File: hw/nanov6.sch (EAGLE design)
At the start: 28 parts, among them CON1 503548-1220, J1 M08X2, Q4 BSS138, U1 TPS622XX

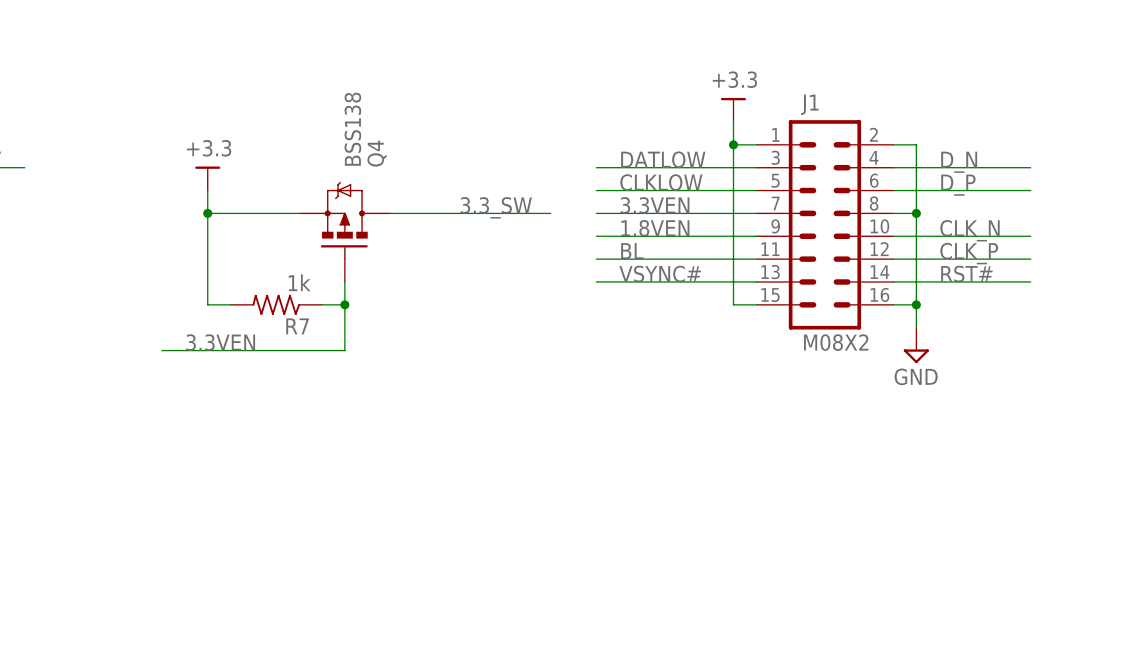
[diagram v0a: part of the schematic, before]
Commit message: add pulldown to RST#, make 3.3VEN active-high. Resolves #471, refs #469.
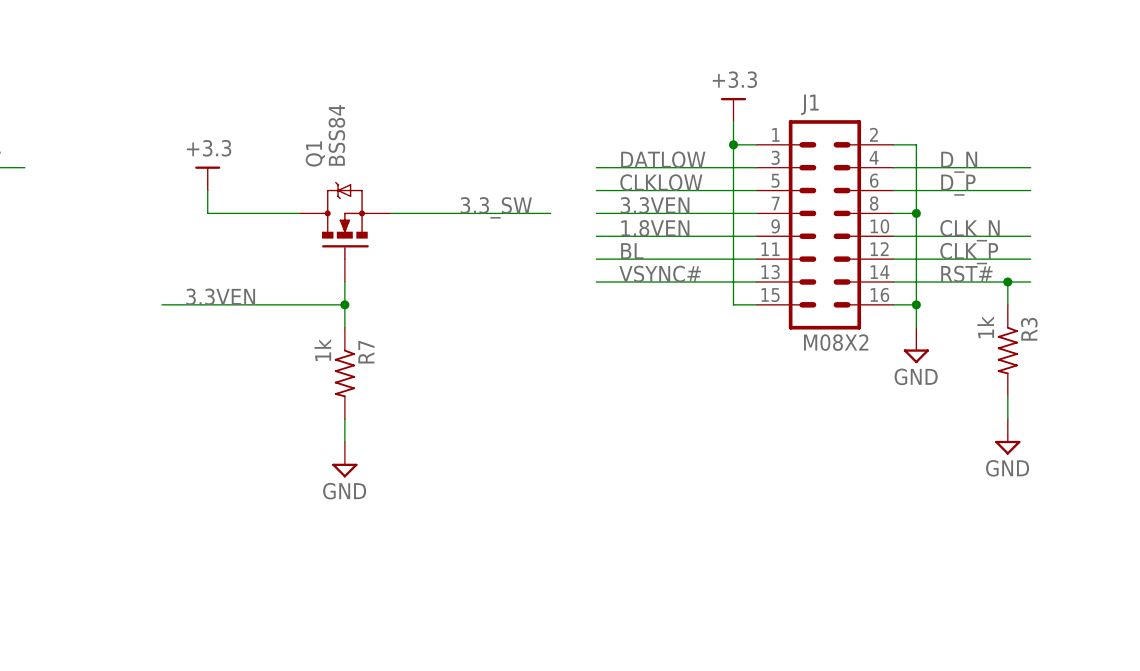
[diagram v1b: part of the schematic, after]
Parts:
- removed Q4: BSS138, SparkFun:MOSFET-PCHANNELSOT23
- added Q1: BSS84, SparkFun:MOSFET-NCHANNELSMD
- added R3: 1k, rcl:R-US_R0805
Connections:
- net +3.3: now also Q1.D; no longer Q4.S, R7.2
- net 3.3VEN: now also Q1.G; no longer Q4.G
- net 3.3_SW: now also Q1.S; no longer Q4.D
- net GND: now also R3.2, R7.2
- net RST#: now also R3.1
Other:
- moved on the sheet: R7
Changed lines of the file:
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@@
 <part name="R13" library="rcl" deviceset="R-US_" device="R0805" value="0"/>
 <part name="U$4" library="ak-supply" deviceset="+3.3" device=""/>
-<part name="Q4" library="SparkFun" deviceset="MOSFET-PCHANNEL" device="SOT23" value="BSS138"/>
 <part name="R7" library="rcl" deviceset="R-US_" device="R0805" value="1k"/>
 <part name="U2" library="ak-misc" deviceset="TLV61220" device=""/>
@@
 <part name="U$11" library="ak-misc" deviceset="MOUNTING_HOLE" device="125"/>
 <part name="U$15" library="ak-misc" deviceset="MOUNTING_HOLE" device="125"/>
+<part name="Q1" library="SparkFun" deviceset="MOSFET-NCHANNEL" device="SMD" value="BSS84"/>
+<part name="U$16" library="ak-supply" deviceset="GND" device=""/>
+<part name="R3" library="rcl" deviceset="R-US_" device="R0805" value="1k"/>
+<part name="U$17" library="ak-supply" deviceset="GND" device=""/>
 </parts>
 <sheets>
@@
 <instance part="R13" gate="G$1" x="101.6" y="147.32" rot="R180"/>
 <instance part="U$4" gate="G$1" x="208.28" y="152.4"/>
-<instance part="Q4" gate="G$1" x="223.52" y="147.32" rot="MR90"/>
-<instance part="R7" gate="G$1" x="215.9" y="137.16" rot="R180"/>
+<instance part="R7" gate="G$1" x="223.52" y="129.54" rot="R270"/>
 <instance part="U2" gate="G$1" x="137.16" y="106.68"/>
 <instance part="R8" gate="G$1" x="154.94" y="93.98" rot="R270"/>
@@
 <instance part="U$11" gate="G$1" x="134.62" y="30.48"/>
 <instance part="U$15" gate="G$1" x="139.7" y="30.48"/>
+<instance part="Q1" gate="G$1" x="223.52" y="147.32" rot="R90"/>
+<instance part="U$16" gate="G$1" x="223.52" y="119.38"/>
+<instance part="R3" gate="G$1" x="297.18" y="132.08" rot="R270"/>
+<instance part="U$17" gate="G$1" x="297.18" y="121.92"/>
 </instances>
 <busses>
@@
 <junction x="266.7" y="25.4"/>
 </segment>
+<segment>
+<pinref part="U$16" gate="G$1" pin="GND"/>
+<pinref part="R7" gate="G$1" pin="2"/>
+<wire x1="223.52" y1="121.92" x2="223.52" y2="124.46" width="0.1524" layer="91"/>
+</segment>
+<segment>
+<pinref part="U$17" gate="G$1" pin="GND"/>
+<pinref part="R3" gate="G$1" pin="2"/>
+<wire x1="297.18" y1="124.46" x2="297.18" y2="127" width="0.1524" layer="91"/>
+</segment>
 </net>
 <net name="CLKLOW" class="0">
@@
 </segment>
 <segment>
-<pinref part="Q4" gate="G$1" pin="D"/>
 <label x="236.22" y="147.32" size="1.778" layer="95"/>
 <wire x1="228.6" y1="147.32" x2="246.38" y2="147.32" width="0.1524" layer="91"/>
+<pinref part="Q1" gate="G$1" pin="S"/>
 </segment>
 </net>
@@
 <segment>
 <pinref part="J1" gate="G$1" pin="14"/>
-<wire x1="284.48" y1="139.7" x2="299.72" y2="139.7" width="0.1524" layer="91"/>
+<wire x1="284.48" y1="139.7" x2="297.18" y2="139.7" width="0.1524" layer="91"/>
 <label x="289.56" y="139.7" size="1.778" layer="95"/>
+<pinref part="R3" gate="G$1" pin="1"/>
+<wire x1="297.18" y1="139.7" x2="299.72" y2="139.7" width="0.1524" layer="91"/>
+<wire x1="297.18" y1="137.16" x2="297.18" y2="139.7" width="0.1524" layer="91"/>
+<junction x="297.18" y="139.7"/>
 </segment>
 </net>
@@
 </segment>
 <segment>
-<pinref part="Q4" gate="G$1" pin="S"/>
-<pinref part="R7" gate="G$1" pin="2"/>
-<wire x1="210.82" y1="137.16" x2="208.28" y2="137.16" width="0.1524" layer="91"/>
-<wire x1="208.28" y1="137.16" x2="208.28" y2="147.32" width="0.1524" layer="91"/>
 <pinref part="U$4" gate="G$1" pin="+3.3"/>
 <wire x1="208.28" y1="147.32" x2="218.44" y2="147.32" width="0.1524" layer="91"/>
 <wire x1="208.28" y1="149.86" x2="208.28" y2="147.32" width="0.1524" layer="91"/>
-<junction x="208.28" y="147.32"/>
+<pinref part="Q1" gate="G$1" pin="D"/>
 </segment>
 <segment>
@@
 <segment>
 <pinref part="R7" gate="G$1" pin="1"/>
-<wire x1="220.98" y1="137.16" x2="223.52" y2="137.16" width="0.1524" layer="91"/>
-<pinref part="Q4" gate="G$1" pin="G"/>
+<wire x1="223.52" y1="134.62" x2="223.52" y2="137.16" width="0.1524" layer="91"/>
 <wire x1="223.52" y1="139.7" x2="223.52" y2="137.16" width="0.1524" layer="91"/>
-<wire x1="223.52" y1="137.16" x2="223.52" y2="132.08" width="0.1524" layer="91"/>
 <junction x="223.52" y="137.16"/>
-<wire x1="223.52" y1="132.08" x2="203.2" y2="132.08" width="0.1524" layer="91"/>
-<label x="205.74" y="132.08" size="1.778" layer="95"/>
-</segment>
-<segment>
+<wire x1="223.52" y1="137.16" x2="203.2" y2="137.16" width="0.1524" layer="91"/>
+<label x="205.74" y="137.16" size="1.778" layer="95"/>
+<pinref part="Q1" gate="G$1" pin="G"/>
+</segment>
+<segment>

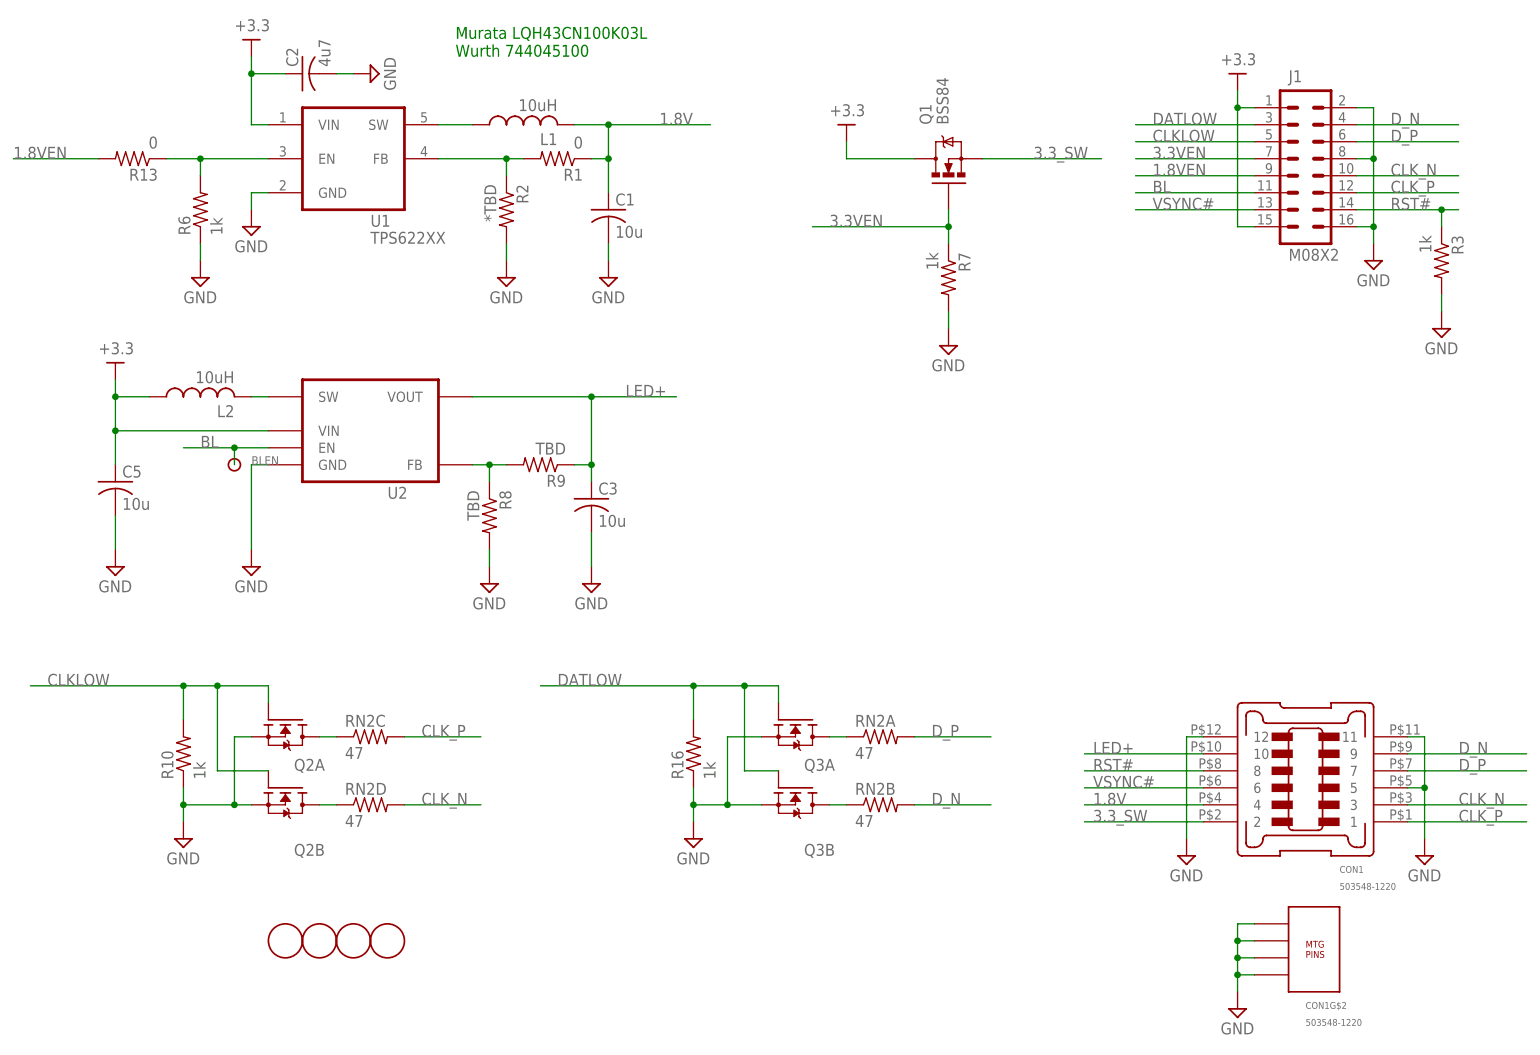
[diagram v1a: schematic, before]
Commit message: add pulldown to BLEN. Resolves #469.
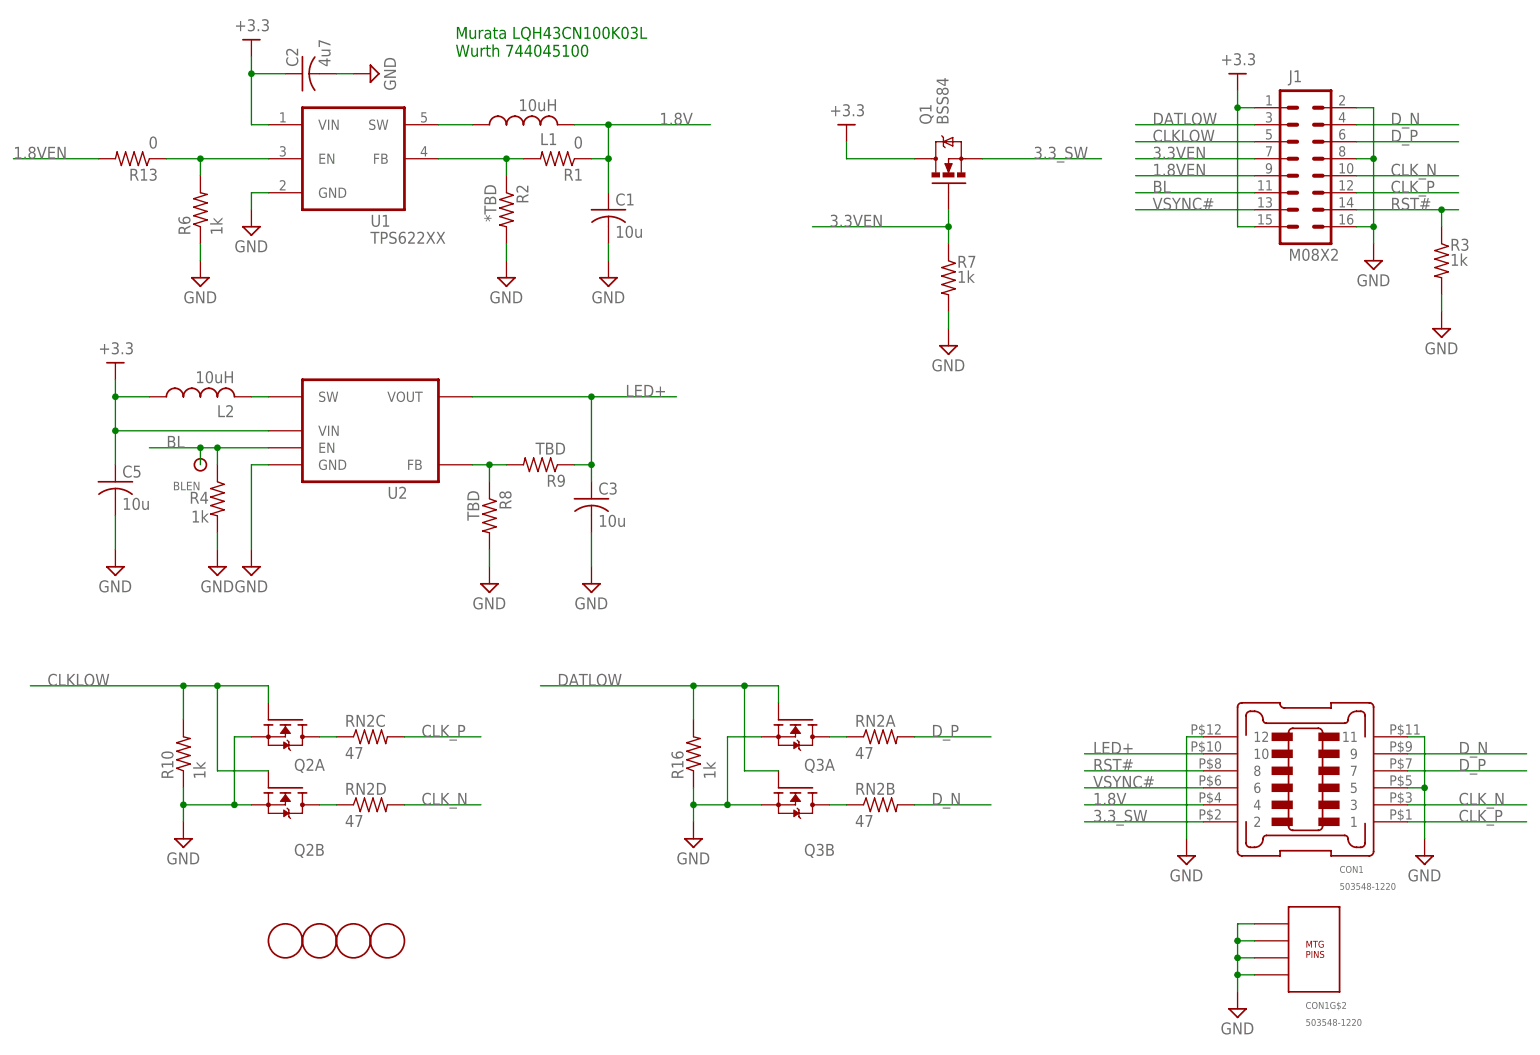
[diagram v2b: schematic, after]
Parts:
- added R4: 1k, rcl:R-US_R0805
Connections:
- net BL: now also R4.1
- net GND: now also R4.2
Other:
- moved on the sheet: BLEN
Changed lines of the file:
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@@
 <part name="R3" library="rcl" deviceset="R-US_" device="R0805" value="1k"/>
 <part name="U$17" library="ak-supply" deviceset="GND" device=""/>
+<part name="R4" library="rcl" deviceset="R-US_" device="R0805" value="1k"/>
+<part name="U$18" library="ak-supply" deviceset="GND" device=""/>
 </parts>
 <sheets>
@@
 <instance part="R13" gate="G$1" x="101.6" y="147.32" rot="R180"/>
 <instance part="U$4" gate="G$1" x="208.28" y="152.4"/>
-<instance part="R7" gate="G$1" x="223.52" y="129.54" rot="R270"/>
+<instance part="R7" gate="G$1" x="223.52" y="129.54" smashed="yes" rot="R270">
+<attribute name="NAME" x="224.79" y="131.0386" size="1.778" layer="95"/>
+<attribute name="VALUE" x="224.79" y="128.778" size="1.778" layer="96"/>
+</instance>
 <instance part="U2" gate="G$1" x="137.16" y="106.68"/>
 <instance part="R8" gate="G$1" x="154.94" y="93.98" rot="R270"/>
@@
 <instance part="U$13" gate="G$1" x="99.06" y="116.84"/>
 <instance part="U$14" gate="G$1" x="266.7" y="160.02"/>
-<instance part="BLEN" gate="1" x="116.84" y="101.6"/>
+<instance part="BLEN" gate="1" x="111.76" y="101.6" smashed="yes">
+<attribute name="NAME" x="111.76" y="99.06" size="1.27" layer="96" rot="R180"/>
+</instance>
 <instance part="CON1" gate="G$2" x="276.86" y="27.94"/>
 <instance part="U$5" gate="G$1" x="266.7" y="20.32"/>
@@
 <instance part="Q1" gate="G$1" x="223.52" y="147.32" rot="R90"/>
 <instance part="U$16" gate="G$1" x="223.52" y="119.38"/>
-<instance part="R3" gate="G$1" x="297.18" y="132.08" rot="R270"/>
+<instance part="R3" gate="G$1" x="297.18" y="132.08" smashed="yes" rot="R270">
+<attribute name="NAME" x="298.45" y="133.5786" size="1.778" layer="95"/>
+<attribute name="VALUE" x="298.45" y="131.318" size="1.778" layer="96"/>
+</instance>
 <instance part="U$17" gate="G$1" x="297.18" y="121.92"/>
+<instance part="R4" gate="G$1" x="114.3" y="96.52" smashed="yes" rot="R270">
+<attribute name="NAME" x="113.03" y="97.5614" size="1.778" layer="95" rot="R180"/>
+<attribute name="VALUE" x="113.03" y="94.742" size="1.778" layer="96" rot="R180"/>
+</instance>
+<instance part="U$18" gate="G$1" x="114.3" y="86.36"/>
 </instances>
 <busses>
@@
 <wire x1="297.18" y1="124.46" x2="297.18" y2="127" width="0.1524" layer="91"/>
 </segment>
+<segment>
+<pinref part="R4" gate="G$1" pin="2"/>
+<pinref part="U$18" gate="G$1" pin="GND"/>
+<wire x1="114.3" y1="91.44" x2="114.3" y2="88.9" width="0.1524" layer="91"/>
+</segment>
 </net>
 <net name="CLKLOW" class="0">
@@
 <segment>
 <pinref part="U2" gate="G$1" pin="EN"/>
-<wire x1="121.92" y1="104.14" x2="116.84" y2="104.14" width="0.1524" layer="91"/>
-<label x="111.76" y="104.14" size="1.778" layer="95"/>
+<wire x1="121.92" y1="104.14" x2="114.3" y2="104.14" width="0.1524" layer="91"/>
+<label x="106.68" y="104.14" size="1.778" layer="95"/>
 <pinref part="BLEN" gate="1" pin="1"/>
-<wire x1="116.84" y1="104.14" x2="109.22" y2="104.14" width="0.1524" layer="91"/>
-<wire x1="116.84" y1="101.6" x2="116.84" y2="104.14" width="0.1524" layer="91"/>
-<junction x="116.84" y="104.14"/>
-</segment>
-<segment>
+<wire x1="114.3" y1="104.14" x2="111.76" y2="104.14" width="0.1524" layer="91"/>
+<wire x1="111.76" y1="104.14" x2="104.14" y2="104.14" width="0.1524" layer="91"/>
+<wire x1="111.76" y1="101.6" x2="111.76" y2="104.14" width="0.1524" layer="91"/>
+<junction x="111.76" y="104.14"/>
+<pinref part="R4" gate="G$1" pin="1"/>
+<wire x1="114.3" y1="101.6" x2="114.3" y2="104.14" width="0.1524" layer="91"/>
+<junction x="114.3" y="104.14"/>
+</segment>
+<segment>
